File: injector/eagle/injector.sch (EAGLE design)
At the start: 34 parts, among them J4 ICSP, U1 ATA6631, U2 ATMEGA328, U3 ATA6631, X1 16MHz

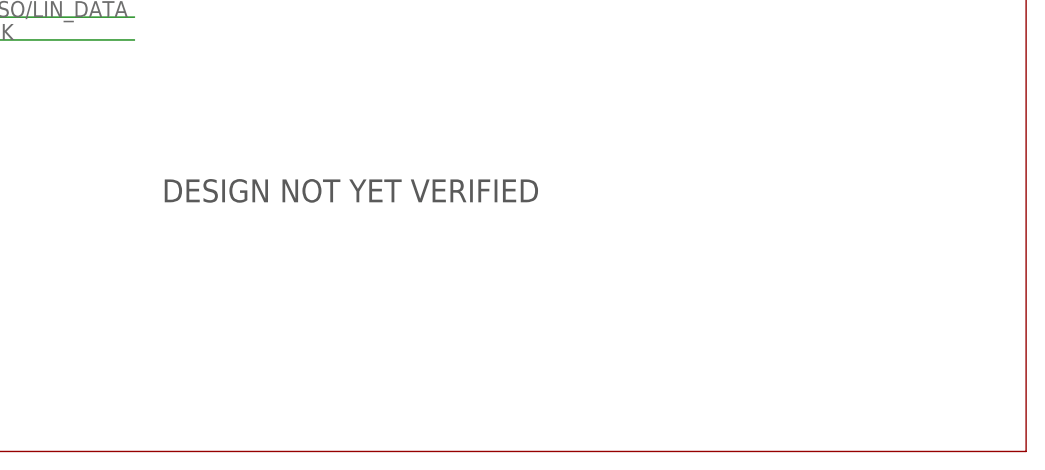
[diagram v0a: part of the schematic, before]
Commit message: Fork the prototype software for the injector.
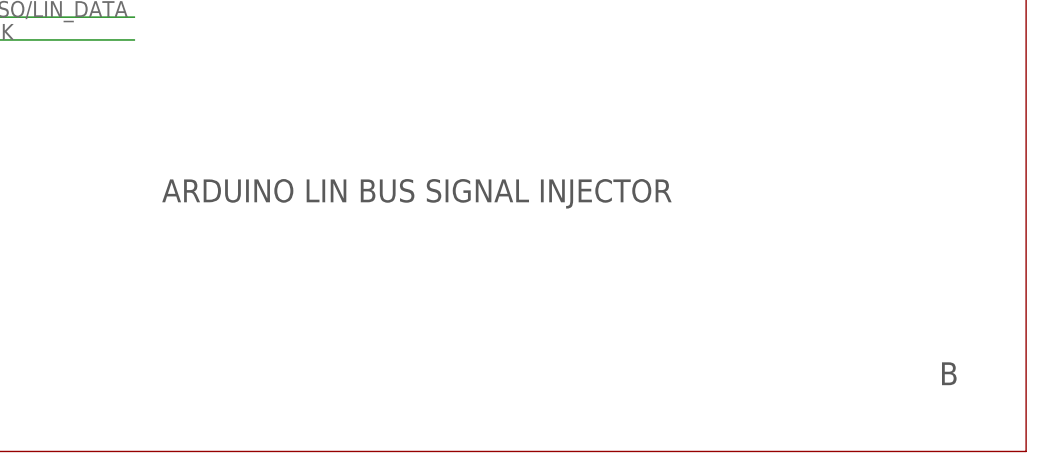
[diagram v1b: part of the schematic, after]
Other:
- note added: "ARDUINO LIN BUS SIGNAL INJECTOR"
- note added: "B"
- note removed: "DESIGN NOT YET VERIFIED"
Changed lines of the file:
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@@
 <text x="55.88" y="81.28" size="2.54" layer="97">SERIAL I/O (Optional)</text>
 <wire x1="33.02" y1="25.4" x2="33.02" y2="213.36" width="0.1524" layer="94"/>
-<text x="213.868" y="53.086" size="2.54" layer="97">DESIGN NOT YET VERIFIED</text>
+<text x="213.868" y="53.086" size="2.54" layer="97">ARDUINO LIN BUS SIGNAL INJECTOR</text>
 <text x="220.218" y="188.468" size="1.27" layer="97">MASTER
 MODE</text>
@@
 <text x="138.938" y="188.468" size="1.27" layer="97">SLAVE
 MODE</text>
+<text x="300.228" y="32.766" size="2.54" layer="97">B</text>
 </plain>
 <instances>
